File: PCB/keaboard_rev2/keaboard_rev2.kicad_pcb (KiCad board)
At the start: 2 copper layers, 141.9 x 93.7 mm, 61 parts, among them K01 KEYSW, K02 KEYSW, K03 KEYSW, K04 KEYSW, K05 KEYSW, K06 KEYSW, K07 KEYSW, K08 KEYSW, K09 KEYSW, K10 KEYSW, K11 KEYSW, K12 KEYSW, K13 KEYSW, K14 KEYSW, K15 KEYSW, K16 KEYSW, K17 KEYSW, K18 KEYSW, K19 KEYSW, K20 KEYSW, K21 KEYSW, K22 KEYSW, K23 KEYSW, K24 KEYSW, K25 KEYSW, U1 ProMicro

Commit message: WIP rev2
Just traces remaining
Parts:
- removed BAT1: Battery, parts:DF3A-3P-2DS_reversible
- removed D01, D02, D03, D04, D05, D06, D07, D08, D09: D, parts:D_SOD123_reversible
- removed K01, K02, K03, K04, K05, K06, K07, K08, K09, K10, K11, K12, K13, K14, K15, K16, K17, K18, K19, K20, K21, K22, K23, K24, K25: KEYSW, parts:Kailh_socket_MX_reversible
- removed REF** (x6): MountingHole_2.2mm_M2, MountingHole:MountingHole_2.2mm_M2
- removed SW_PWR1: SW_Push_SPDT, parts:SW_PCM12SMTR_reversible
- removed SW_RST1: SW_EVQ-9P701P, parts:SW_EVQ-9P701P_reversible
- removed TRRS1: TRRS Jack, parts:TRRS-PJ-320A_reversible
- added D1: 1N4148W, parts:D_SOD123_reversible, F.Cu at (63.2, 53.3)
- added D2: 1N4148W, parts:D_SOD123_reversible, F.Cu at (63.2, 72.3)
- added D3: 1N4148W, parts:D_SOD123_reversible, F.Cu at (63.2, 91.4)
- added D4: 1N4148W, parts:D_SOD123_reversible, F.Cu at (63.2, 110.4)
- added D5: 1N4148W, parts:D_SOD123_reversible, F.Cu at (82.3, 50.7)
- added D6: 1N4148W, parts:D_SOD123_reversible, F.Cu at (82.3, 69.8)
- added D7: 1N4148W, parts:D_SOD123_reversible, F.Cu at (82.3, 88.8)
- added D8: 1N4148W, parts:D_SOD123_reversible, F.Cu at (82.3, 107.9)
- added D9: 1N4148W, parts:D_SOD123_reversible, F.Cu at (101.3, 48.2)
- added J1: AudioJack4, parts:TRRS-PJ-320A_reversible, F.Cu at (185.7, 81.2)
- added LED1: SK6812MINI, parts:YS-SK6812MINI-E_reversible, F.Cu at (55.1, 52.4)
- added LED10: SK6812MINI, parts:YS-SK6812MINI-E_reversible, F.Cu at (93.2, 66.4)
- added LED11: SK6812MINI, parts:YS-SK6812MINI-E_reversible, F.Cu at (93.2, 85.4)
- added LED12: SK6812MINI, parts:YS-SK6812MINI-E_reversible, F.Cu at (93.2, 104.5)
- added LED13: SK6812MINI, parts:YS-SK6812MINI-E_reversible, F.Cu at (112.3, 44.8)
- added LED14: SK6812MINI, parts:YS-SK6812MINI-E_reversible, F.Cu at (112.3, 63.8)
- added LED15: SK6812MINI, parts:YS-SK6812MINI-E_reversible, F.Cu at (112.3, 82.9)
- added LED16: SK6812MINI, parts:YS-SK6812MINI-E_reversible, F.Cu at (112.3, 101.9)
- added LED17: SK6812MINI, parts:YS-SK6812MINI-E_reversible, F.Cu at (131.3, 47.3)
- added LED18: SK6812MINI, parts:YS-SK6812MINI-E_reversible, F.Cu at (131.3, 66.4)
- added LED19: SK6812MINI, parts:YS-SK6812MINI-E_reversible, F.Cu at (131.3, 85.4)
- added LED2: SK6812MINI, parts:YS-SK6812MINI-E_reversible, F.Cu at (55.1, 71.5)
- added LED20: SK6812MINI, parts:YS-SK6812MINI-E_reversible, F.Cu at (141.8, 106.6)
- added LED21: SK6812MINI, parts:YS-SK6812MINI-E_reversible, F.Cu at (150.4, 49.9)
- added LED22: SK6812MINI, parts:YS-SK6812MINI-E_reversible, F.Cu at (150.4, 68.9)
- added LED23: SK6812MINI, parts:YS-SK6812MINI-E_reversible, F.Cu at (150.4, 88.0)
- added LED24: SK6812MINI, parts:YS-SK6812MINI-E_reversible, F.Cu at (172.8, 95.9)
- added LED25: SK6812MINI, parts:YS-SK6812MINI-E_reversible, F.Cu at (166.3, 113.8)
- added LED3: SK6812MINI, parts:YS-SK6812MINI-E_reversible, F.Cu at (55.1, 90.5)
- added LED4: SK6812MINI, parts:YS-SK6812MINI-E_reversible, F.Cu at (55.1, 109.6)
- added LED5: SK6812MINI, parts:YS-SK6812MINI-E_reversible, F.Cu at (74.2, 49.9)
- added LED6: SK6812MINI, parts:YS-SK6812MINI-E_reversible, F.Cu at (74.2, 68.9)
- added LED7: SK6812MINI, parts:YS-SK6812MINI-E_reversible, F.Cu at (74.2, 88.0)
- added LED8: SK6812MINI, parts:YS-SK6812MINI-E_reversible, F.Cu at (74.2, 107.0)
- added LED9: SK6812MINI, parts:YS-SK6812MINI-E_reversible, F.Cu at (93.2, 47.3)
- added RESET1: SW_Push, parts:SW_EVQ-9P701P_reversible, F.Cu at (157.5, 41.0)
- added SW1: SW_Push, keyswitches:Kailh_socket_PG1350_reversible, F.Cu at (55.1, 57.1)
- added SW10: SW_Push, keyswitches:Kailh_socket_PG1350_reversible, F.Cu at (93.2, 71.1)
- added SW11: SW_Push, keyswitches:Kailh_socket_PG1350_reversible, F.Cu at (93.2, 90.1)
- added SW12: SW_Push, keyswitches:Kailh_socket_PG1350_reversible, F.Cu at (93.2, 109.2)
- added SW13: SW_Push, keyswitches:Kailh_socket_PG1350_reversible, F.Cu at (112.3, 49.5)
- added SW14: SW_Push, keyswitches:Kailh_socket_PG1350_reversible, F.Cu at (112.3, 68.5)
- added SW15: SW_Push, keyswitches:Kailh_socket_PG1350_reversible, F.Cu at (112.3, 87.6)
- added SW16: SW_Push, keyswitches:Kailh_socket_PG1350_reversible, F.Cu at (112.3, 106.6)
- added SW17: SW_Push, keyswitches:Kailh_socket_PG1350_reversible, F.Cu at (131.3, 52.0)
- added SW18: SW_Push, keyswitches:Kailh_socket_PG1350_reversible, F.Cu at (131.3, 71.1)
- added SW19: SW_Push, keyswitches:Kailh_socket_PG1350_reversible, F.Cu at (131.3, 90.1)
- added SW2: SW_Push, keyswitches:Kailh_socket_PG1350_reversible, F.Cu at (55.1, 76.1)
- added SW20: SW_Push, keyswitches:Kailh_socket_PG1350_reversible, F.Cu at (141.0, 111.2)
- added SW21: SW_Push, keyswitches:Kailh_socket_PG1350_reversible, F.Cu at (150.4, 54.6)
- added SW22: SW_Push, keyswitches:Kailh_socket_PG1350_reversible, F.Cu at (150.4, 73.6)
- added SW23: SW_Push, keyswitches:Kailh_socket_PG1350_reversible, F.Cu at (150.4, 92.7)
- added SW24: SW_Push, keyswitches:Kailh_socket_PG1350_reversible, F.Cu at (171.2, 100.4)
- added SW25: SW_Push, keyswitches:Kailh_socket_PG1350_reversible, F.Cu at (164.7, 118.3)
- added SW3: SW_Push, keyswitches:Kailh_socket_PG1350_reversible, F.Cu at (55.1, 95.2)
- added SW4: SW_Push, keyswitches:Kailh_socket_PG1350_reversible, F.Cu at (55.1, 114.2)
- added SW5: SW_Push, keyswitches:Kailh_socket_PG1350_reversible, F.Cu at (74.2, 54.6)
- added SW6: SW_Push, keyswitches:Kailh_socket_PG1350_reversible, F.Cu at (74.2, 73.6)
- added SW7: SW_Push, keyswitches:Kailh_socket_PG1350_reversible, F.Cu at (74.2, 92.7)
- added SW8: SW_Push, keyswitches:Kailh_socket_PG1350_reversible, F.Cu at (74.2, 111.7)
- added SW9: SW_Push, keyswitches:Kailh_socket_PG1350_reversible, F.Cu at (93.2, 52.0)
- D10, D11, D12, D13, D14, D15, D16, D17, D18, D19, D20, D21, D22, D23, D24, D25: value D -> 1N4148W
- moved D20 33.6 mm to (149.7, 108.9), turned to 80 degrees
- moved D25 32.3 mm to (173.8, 117.5), turned to 70 degrees
- moved D24 32.3 mm to (180.3, 99.6), turned to 70 degrees
- moved D21 30.3 mm to (158.5, 50.7), turned to 90 degrees
- moved D22 30.3 mm to (158.5, 69.8), turned to 90 degrees
- moved D23 30.3 mm to (158.5, 88.8), turned to 90 degrees
- moved D14 30.3 mm to (120.4, 64.7), turned to 90 degrees
- moved D15 30.3 mm to (120.4, 83.8), turned to 90 degrees
- moved D16 30.3 mm to (120.4, 102.8), turned to 90 degrees
- moved D13 30.3 mm to (120.4, 45.7), turned to 90 degrees
- moved D17 30.3 mm to (139.4, 48.2), turned to 90 degrees
- moved D10 30.3 mm to (101.3, 67.3), turned to 90 degrees
- moved D11 30.3 mm to (101.3, 86.3), turned to 90 degrees
- moved D12 30.3 mm to (101.3, 105.4), turned to 90 degrees
- moved D18 30.3 mm to (139.4, 67.3), turned to 90 degrees
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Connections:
- D10 pad 1: ROW2 -> Row2
- D11 pad 1: ROW3 -> Row3
- D12 pad 1: ROW4 -> Row4
- D13 pad 1: ROW1 -> Row1
- D14 pad 1: ROW2 -> Row2
- D15 pad 1: ROW3 -> Row3
- D16 pad 1: ROW4 -> Row4
- D17 pad 1: ROW1 -> Row1
- D18 pad 1: ROW2 -> Row2
- D19 pad 1: ROW3 -> Row3
- D20 pad 1: ROW4 -> Row4
- D21 pad 1: ROW1 -> Row1
- D22 pad 1: ROW2 -> Row2
- D23 pad 1: ROW3 -> Row3
- D24 pad 1: ROW3 -> Row3
- D25 pad 1: ROW4 -> Row4
- U1 pad 10: ROW2 -> Row3
- U1 pad 11: ROW3 -> Row4
- U1 pad 12: ROW4 -> Col1
- U1 pad 13: COL7 -> Col2
- U1 pad 14: COL6 -> Col3
- U1 pad 15: COL5 -> Col4
- U1 pad 16: COL4 -> Col5
- U1 pad 17: COL3 -> Col6
- U1 pad 18: COL2 -> Col7
- U1 pad 19: COL1 -> TRRS_T
- U1 pad 20: Net-(U1-Pad20) -> LED
- U1 pad 21: VCC -> Net-(U1-Pad21)
- U1 pad 5: Net-(U1-Pad5) -> TRRS_R2
- U1 pad 6: SOFT_SERIAL_PIN -> Net-(U1-Pad6)
- U1 pad 8: Net-(U1-Pad8) -> Row1
- U1 pad 9: ROW1 -> Row2
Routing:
- net COL1: track 247.3 -> 0.00 mm, vias 4 -> 0
- net COL2: track 219.5 -> 0.00 mm, vias 4 -> 0
- net COL3: track 214.3 -> 0.00 mm, vias 4 -> 0
- net ROW4: track 207.2 -> 0.00 mm, vias 7 -> 0
- net ROW3: track 192.5 -> 0.00 mm, vias 8 -> 0
- net COL4: track 191.4 -> 0.00 mm, vias 4 -> 0
- net COL5: track 177.0 -> 0.00 mm, vias 4 -> 0
- net ROW2: track 148.5 -> 0.00 mm, vias 7 -> 0
- net ROW1: track 140.4 -> 0.00 mm, vias 7 -> 0
- net COL6: track 119.5 -> 0.00 mm, vias 3 -> 0
- net GND: track 111.3 -> 0.00 mm, vias 6 -> 0
- net COL7: track 90.1 -> 0.00 mm, vias 2 -> 0
- net RAW: track 76.3 -> 0.00 mm, vias 1 -> 0
- net VCC: track 51.5 -> 0.00 mm
- net SOFT_SERIAL_PIN: track 47.0 -> 0.00 mm, vias 1 -> 0
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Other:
- net class Default: trace_width 0.254 -> 0.25
- net class Power removed
- rule pad_to_mask_clearance: 0.05 -> 0
- board text added: "LED"
- board text added: "rev2"
- board text removed: "rev1"

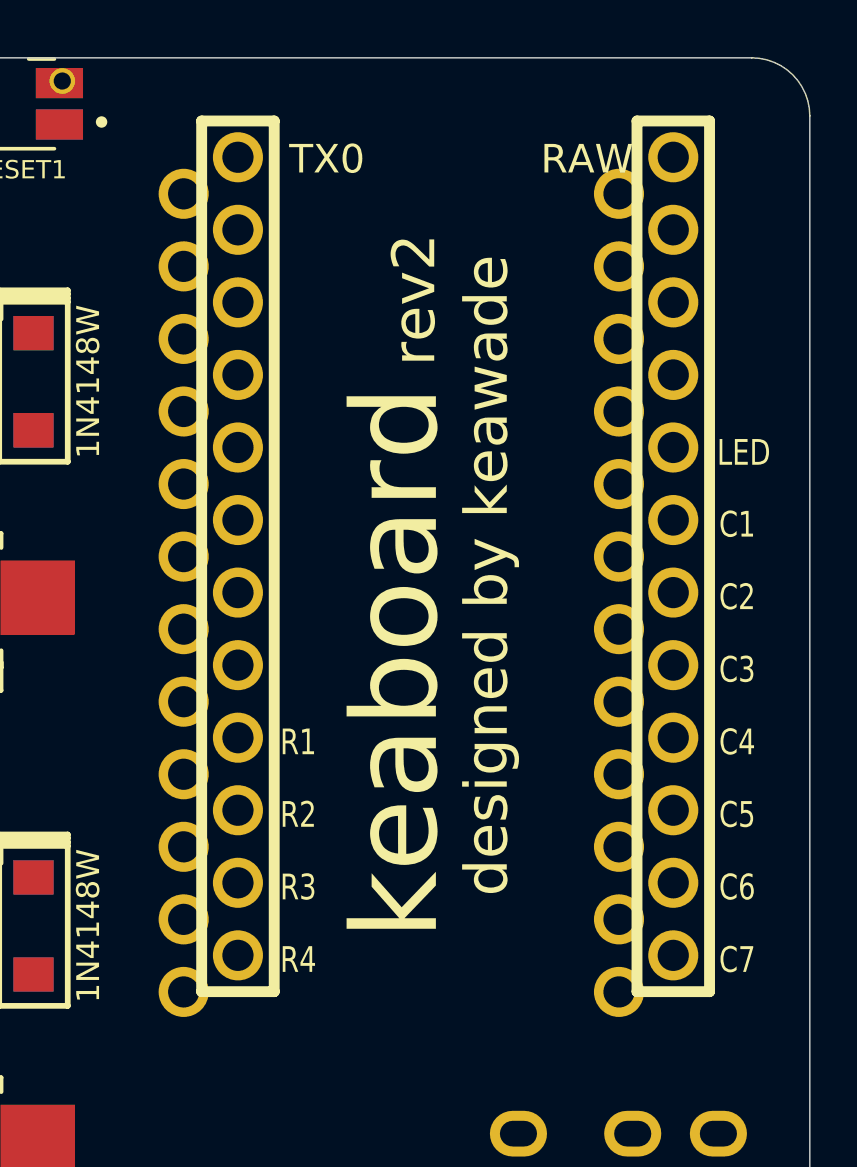
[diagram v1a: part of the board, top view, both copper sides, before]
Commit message: Fix schematic/net mistake from old rev1 pdf
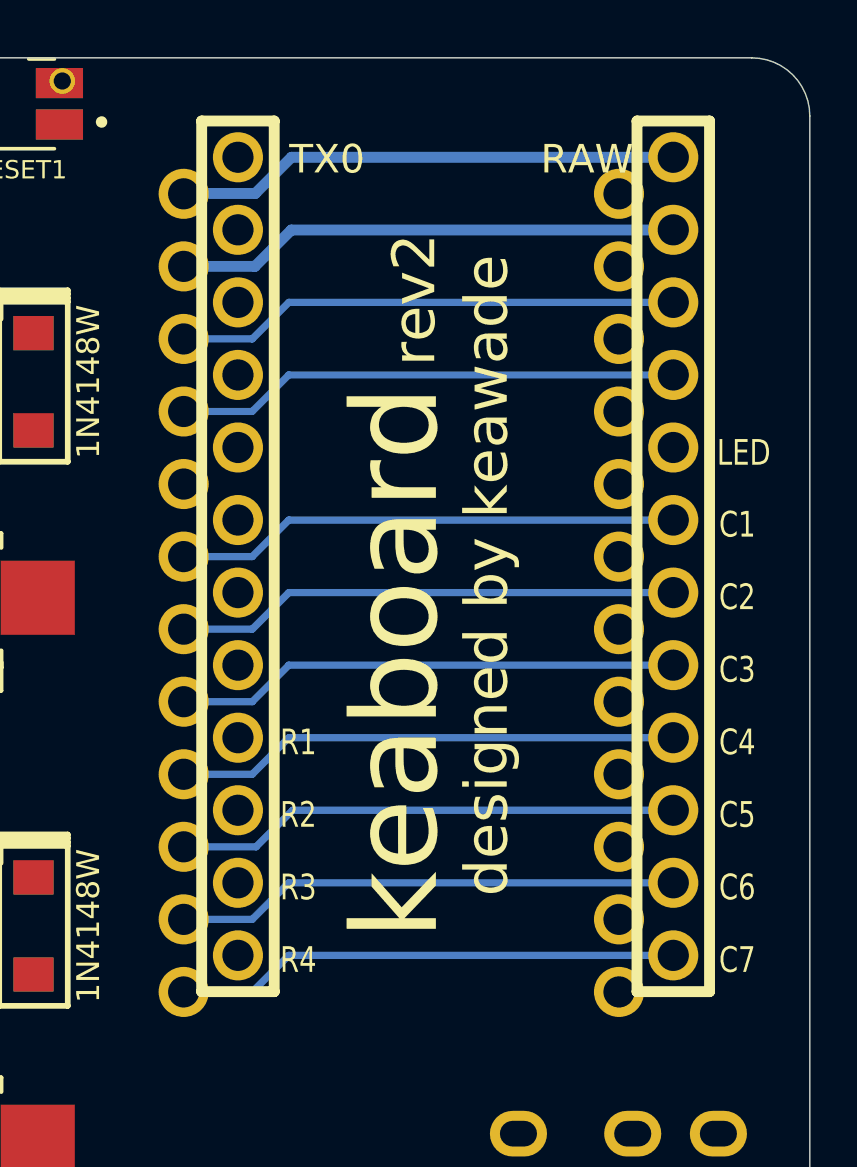
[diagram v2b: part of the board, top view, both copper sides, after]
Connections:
- U1 pad 10: Row3 -> Row2
- U1 pad 11: Row4 -> Row3
- U1 pad 12: Col1 -> Row4
- U1 pad 13: Col2 -> Col7
- U1 pad 14: Col3 -> Col6
- U1 pad 15: Col4 -> Col5
- U1 pad 16: Col5 -> Col4
- U1 pad 17: Col6 -> Col3
- U1 pad 18: Col7 -> Col2
- U1 pad 19: TRRS_T -> Col1
- U1 pad 20: LED -> Net-(U1-Pad20)
- U1 pad 21: Net-(U1-Pad21) -> TRRS_R2
- U1 pad 5: TRRS_R2 -> Net-(U1-Pad5)
- U1 pad 6: Net-(U1-Pad6) -> TRRS_T
- U1 pad 8: Row1 -> LED
- U1 pad 9: Row2 -> Row1
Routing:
- net RAW: track 0.00 -> 17.7 mm
- net GND: track 0.00 -> 17.7 mm
- net TRRS_R2: track 0.00 -> 17.7 mm
- net RESET: track 0.00 -> 17.7 mm
- net Col7: track 0.00 -> 17.7 mm
- net Col6: track 0.00 -> 17.7 mm
- net Col5: track 0.00 -> 17.7 mm
- net Col4: track 0.00 -> 17.7 mm
- net Col3: track 0.00 -> 17.7 mm
- net Col2: track 0.00 -> 17.7 mm
- net Col1: track 0.00 -> 17.7 mm

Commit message: Export DSN
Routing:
- net RAW: track 17.7 -> 0.00 mm
- net GND: track 17.7 -> 0.00 mm
- net TRRS_R2: track 17.7 -> 0.00 mm
- net RESET: track 17.7 -> 0.00 mm
- net Col7: track 17.7 -> 0.00 mm
- net Col6: track 17.7 -> 0.00 mm
- net Col5: track 17.7 -> 0.00 mm
- net Col4: track 17.7 -> 0.00 mm
- net Col3: track 17.7 -> 0.00 mm
- net Col2: track 17.7 -> 0.00 mm
- net Col1: track 17.7 -> 0.00 mm

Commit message: Set up net classes
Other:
- net class Default: trace_width 0.25 -> 0.254
- net class Heavy added: clearance 0.2, trace_width 0.381, via_dia 0.8, via_drill 0.4
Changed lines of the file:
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@@
   )
   (setup
-    (last_trace_width 0.25)
+    (last_trace_width 0.254)
     (user_trace_width 0.254)
     (user_trace_width 0.381)
@@
   (net_class Default "This is the default net class."
     (clearance 0.2)
-    (trace_width 0.25)
+    (trace_width 0.254)
     (via_dia 0.8)
     (via_drill 0.4)
@@
     (add_net Col6)
     (add_net Col7)
-    (add_net GND)
     (add_net LED)
     (add_net "Net-(D1-Pad2)")
@@
     (add_net "Net-(U1-Pad5)")
     (add_net "Net-(U1-Pad7)")
-    (add_net RAW)
     (add_net RESET)
     (add_net Row1)
@@
     (add_net TRRS_T)
   )
+  (net_class Heavy ""
+    (clearance 0.2)
+    (trace_width 0.381)
+    (via_dia 0.8)
+    (via_drill 0.4)
+    (uvia_dia 0.3)
+    (uvia_drill 0.1)
+    (add_net GND)
+    (add_net RAW)
+  )
   (module parts:ArduinoProMicro_Reversible (layer F.Cu)

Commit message: Fix issue where kicad could not determine board outline
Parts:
- D1: value 1N4148W -> D1
- D10: value 1N4148W -> D10
- D11: value 1N4148W -> D11
- D12: value 1N4148W -> D12
- D13: value 1N4148W -> D13
- D14: value 1N4148W -> D14
- D15: value 1N4148W -> D15
- D16: value 1N4148W -> D16
- D17: value 1N4148W -> D17
- D18: value 1N4148W -> D18
- D19: value 1N4148W -> D19
- D2: value 1N4148W -> D2
- D20: value 1N4148W -> D20
- D21: value 1N4148W -> D21
- D22: value 1N4148W -> D22
- D23: value 1N4148W -> D23
- D24: value 1N4148W -> D24
- D25: value 1N4148W -> D25
- D3: value 1N4148W -> D3
- D4: value 1N4148W -> D4
- D5: value 1N4148W -> D5
- D6: value 1N4148W -> D6
- D7: value 1N4148W -> D7
- D8: value 1N4148W -> D8
- D9: value 1N4148W -> D9
- renumbered RESET1 to RESET

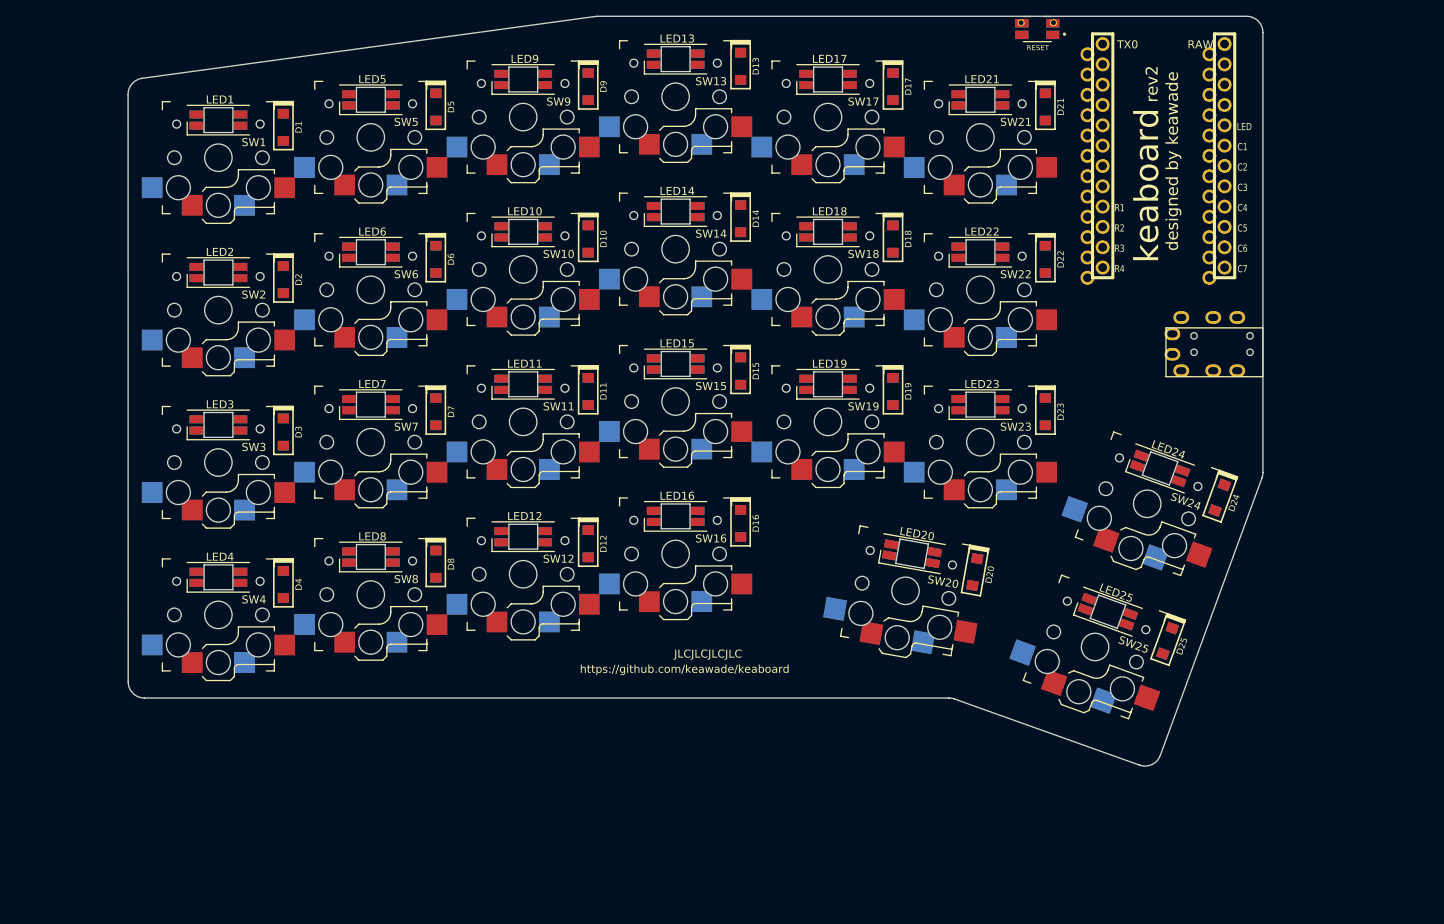
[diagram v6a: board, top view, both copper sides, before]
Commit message: Reorder LEDs in schematic for better routing
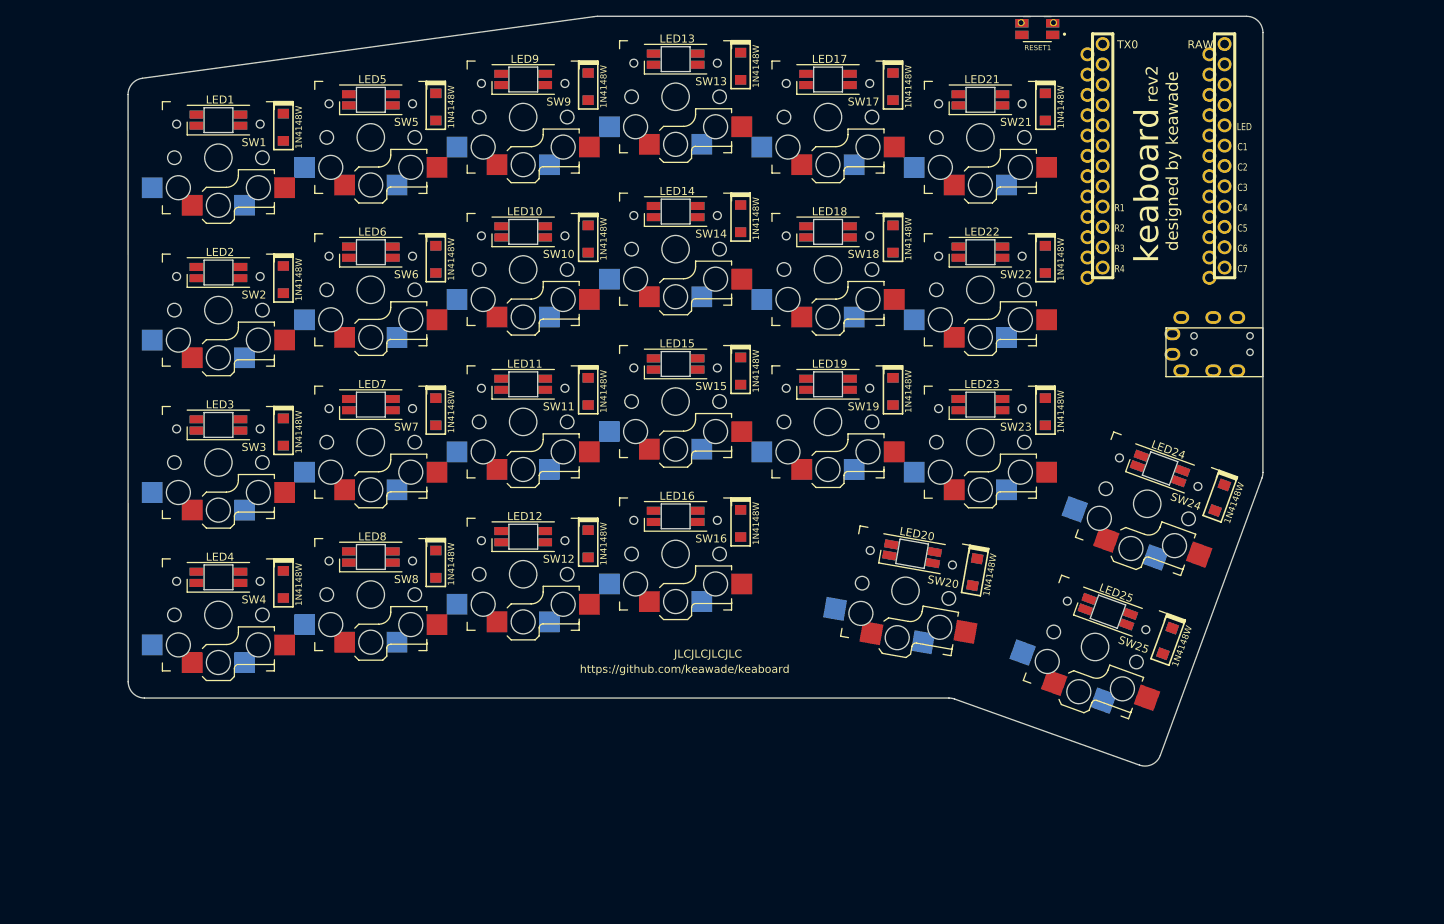
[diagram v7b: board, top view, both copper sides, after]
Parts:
- D1: value D1 -> 1N4148W
- D10: value D10 -> 1N4148W
- D11: value D11 -> 1N4148W
- D12: value D12 -> 1N4148W
- D13: value D13 -> 1N4148W
- D14: value D14 -> 1N4148W
- D15: value D15 -> 1N4148W
- D16: value D16 -> 1N4148W
- D17: value D17 -> 1N4148W
- D18: value D18 -> 1N4148W
- D19: value D19 -> 1N4148W
- D2: value D2 -> 1N4148W
- D20: value D20 -> 1N4148W
- D21: value D21 -> 1N4148W
- D22: value D22 -> 1N4148W
- D23: value D23 -> 1N4148W
- D24: value D24 -> 1N4148W
- D25: value D25 -> 1N4148W
- D3: value D3 -> 1N4148W
- D4: value D4 -> 1N4148W
- D5: value D5 -> 1N4148W
- D6: value D6 -> 1N4148W
- D7: value D7 -> 1N4148W
- D8: value D8 -> 1N4148W
- D9: value D9 -> 1N4148W
- renumbered RESET to RESET1
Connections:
- LED1 pad 3: LED -> Net-(LED1-Pad3)
- LED11 pad 3: Net-(LED10-Pad1) -> Net-(LED11-Pad3)
- LED12 pad 3: Net-(LED11-Pad1) -> Net-(LED12-Pad3)
- LED13 pad 3: Net-(LED12-Pad1) -> Net-(LED13-Pad3)
- LED14 pad 3: Net-(LED13-Pad1) -> Net-(LED10-Pad1)
- LED15 pad 1: Net-(LED15-Pad1) -> Net-(LED11-Pad3)
- LED15 pad 3: Net-(LED14-Pad1) -> Net-(LED15-Pad3)
- LED16 pad 3: Net-(LED15-Pad1) -> Net-(LED12-Pad1)
- LED17 pad 1: Net-(LED17-Pad1) -> Net-(LED13-Pad3)
- LED17 pad 3: Net-(LED16-Pad1) -> Net-(LED17-Pad3)
- LED18 pad 3: Net-(LED17-Pad1) -> Net-(LED14-Pad1)
- LED19 pad 1: Net-(LED19-Pad1) -> Net-(LED15-Pad3)
- LED19 pad 3: Net-(LED18-Pad1) -> Net-(LED19-Pad3)
- LED20 pad 3: Net-(LED19-Pad1) -> Net-(LED16-Pad1)
- LED21 pad 1: Net-(LED21-Pad1) -> Net-(LED17-Pad3)
- LED21 pad 3: Net-(LED20-Pad1) -> LED
- LED22 pad 3: Net-(LED21-Pad1) -> Net-(LED18-Pad1)
- LED23 pad 1: Net-(LED23-Pad1) -> Net-(LED19-Pad3)
- LED24 pad 3: Net-(LED23-Pad1) -> Net-(LED24-Pad3)
- LED25 pad 1: Net-(LED25-Pad1) -> Net-(LED24-Pad3)
- LED25 pad 3: Net-(LED24-Pad1) -> Net-(LED20-Pad1)
- LED3 pad 3: Net-(LED2-Pad1) -> Net-(LED3-Pad3)
- LED5 pad 1: Net-(LED5-Pad1) -> Net-(LED1-Pad3)
- LED5 pad 3: Net-(LED4-Pad1) -> Net-(LED5-Pad3)
- LED6 pad 1: Net-(LED6-Pad1) -> Net-(LED10-Pad3)
- LED6 pad 3: Net-(LED5-Pad1) -> Net-(LED6-Pad3)
- LED7 pad 1: Net-(LED7-Pad1) -> Net-(LED3-Pad3)
- LED7 pad 3: Net-(LED6-Pad1) -> Net-(LED11-Pad1)
- LED8 pad 1: Net-(LED8-Pad1) -> Net-(LED12-Pad3)
- LED8 pad 3: Net-(LED7-Pad1) -> Net-(LED4-Pad1)
- LED9 pad 1: Net-(LED10-Pad3) -> Net-(LED5-Pad3)
- LED9 pad 3: Net-(LED8-Pad1) -> Net-(LED13-Pad1)
